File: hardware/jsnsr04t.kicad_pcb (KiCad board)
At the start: 2 copper layers, 50 x 25 mm, 12 parts, among them J1 SWD, J2 MOD_L, J3 JSN-SR04T, J4 MOD_R, U2 DS18B20, U3 5V LDO, U4 TXB0104D, U5 ATtiny1614-SS

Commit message: Route PCB
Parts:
- added G***: LOGO, Logos:logo-pollex-15mm, F.Cu at (108.6, 122.6)
- moved U3 25.1 mm to (138.8, 111.0), turned to 180 degrees
- moved C2 19.9 mm to (136.8, 108.4), turned to 180 degrees
- moved C3 19.7 mm to (135.8, 111.1), turned to 90 degrees
- moved U2 9.00 mm to (134.5, 118.5)
- moved J3 4.00 mm to (124.0, 106.5)
- moved C4 3.35 mm to (116.3, 119.5), turned to 0 degrees
- moved R1 2.52 mm to (125.6, 119.4), turned to 180 degrees
- moved U4 2.50 mm to (121.5, 114.0)
- moved U5 1.73 mm to (113.0, 114.0)
- moved J1 1.07 mm to (107.3, 103.4)
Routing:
- net +3V3: track 0.00 -> 67.7 mm
- net /5V_EN: track 0.00 -> 47.8 mm, vias 0 -> 2
- net +5V?: track 0.00 -> 31.8 mm
- net /SMBALERT: track 0.00 -> 20.1 mm
- net /UPDI: track 0.00 -> 15.5 mm
- net /OneWire_High: track 0.00 -> 14.7 mm
- net GND: track 0.00 -> 12.3 mm, vias 0 -> 8
- net /I2C_SCL: track 0.00 -> 11.4 mm
- net /UART_RX_High: track 0.00 -> 8.90 mm
- net /I2C_SDA: track 0.00 -> 7.18 mm
- net /UART_TX_High: track 0.00 -> 6.58 mm
- net +BATT: track 0.00 -> 6.11 mm
- net /UART_RX_Low: track 0.00 -> 4.08 mm
- net /UART_TX_Low: track 0.00 -> 4.08 mm
- net /OneWire_Low: track 0.00 -> 4.08 mm
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- added copper zone on B.Cu, net GND
- added copper zone on F.Cu, net GND
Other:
- board text added: "+3V3"
- board text added: "ALERT"
- board text added: "DS18B20"
- board text added: "GND"
- board text added: "JSN SR04T"
- board text added: "JSN-SR04T"
- board text added: "SCL"
- board text added: "SDA"
- board text added: "VBAT"

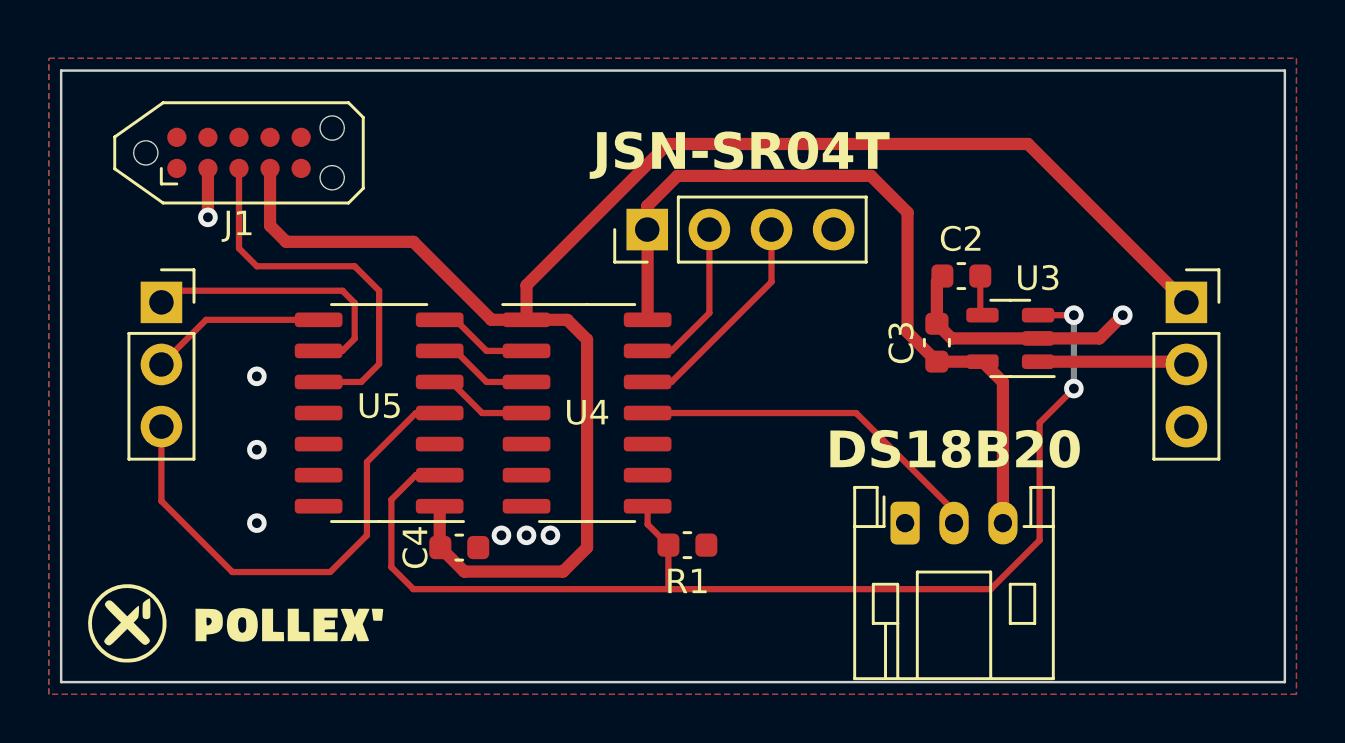
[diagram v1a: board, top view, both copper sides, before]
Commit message: Include terminal blocks for DS18B20
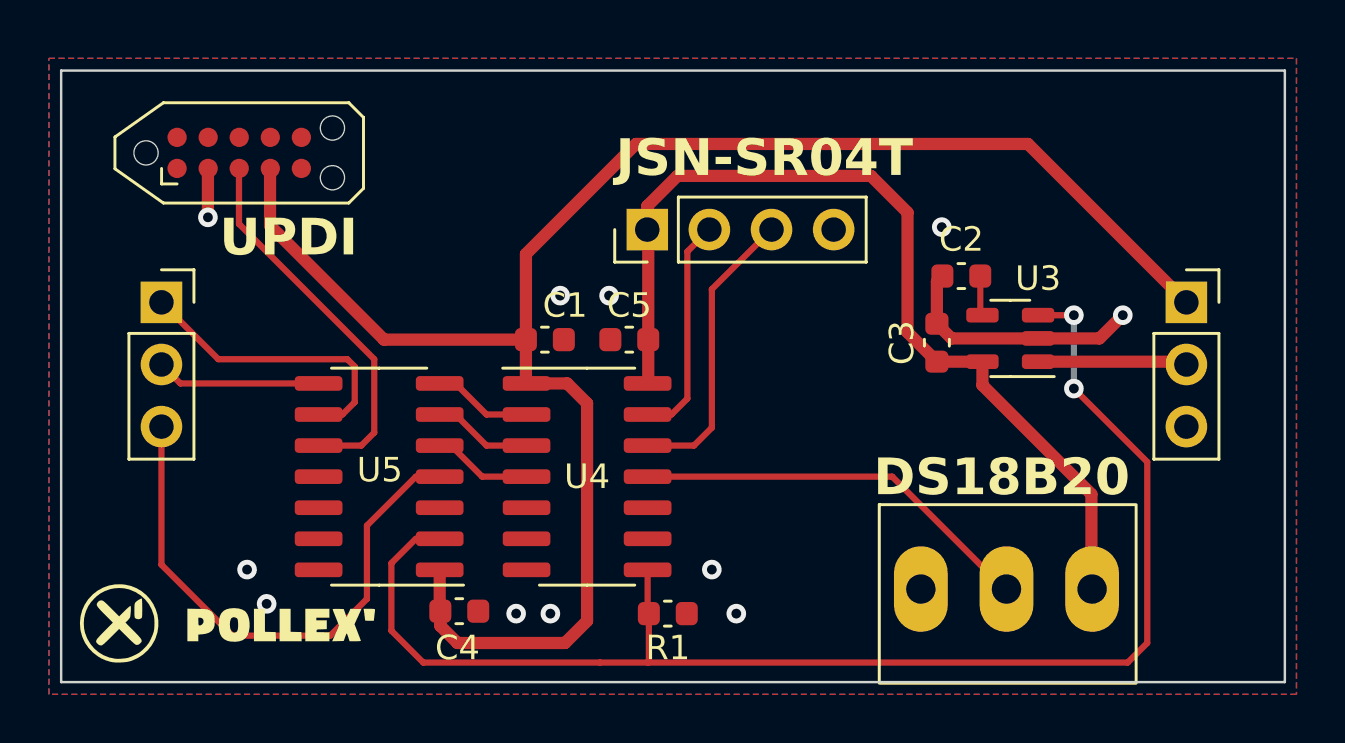
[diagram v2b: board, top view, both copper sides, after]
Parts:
- added C1: 100n, Capacitor_SMD:C_0603_1608Metric, F.Cu at (119.8, 111.0)
- added C5: 100n, Capacitor_SMD:C_0603_1608Metric, F.Cu at (123.2, 111.0)
- U2: footprint Connector_JST:JST_PH_S3B-PH-K_1x03_P2.00mm_Horizontal -> Library:TE-Connectivity_3_pin_terminal_block
- moved R1 2.91 mm to (124.8, 122.2)
- moved C4 2.60 mm to (116.3, 122.1)
- moved U4 2.60 mm to (121.5, 116.6)
- moved U5 2.60 mm to (113.0, 116.6)
- moved U2 1.30 mm to (133.4, 117.7)
- moved G*** 0.33 mm to (108.3, 122.6)
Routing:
- net /5V_EN: track 47.8 -> 56.8 mm
- net +5V?: track 31.8 -> 38.7 mm
- net +3V3: track 67.7 -> 72.3 mm
- net /UART_RX_High: track 8.90 -> 12.0 mm
- net /UART_TX_High: track 6.58 -> 9.18 mm
- net /SMBALERT: track 20.1 -> 22.7 mm
- net /OneWire_High: track 14.7 -> 16.6 mm
- net /I2C_SCL: track 11.4 -> 12.1 mm
- net GND: vias 8 -> 11
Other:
- board text added: "UPDI"

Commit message: Drive DS18B20 from IO Port\nRemove DS18B20 from level translator
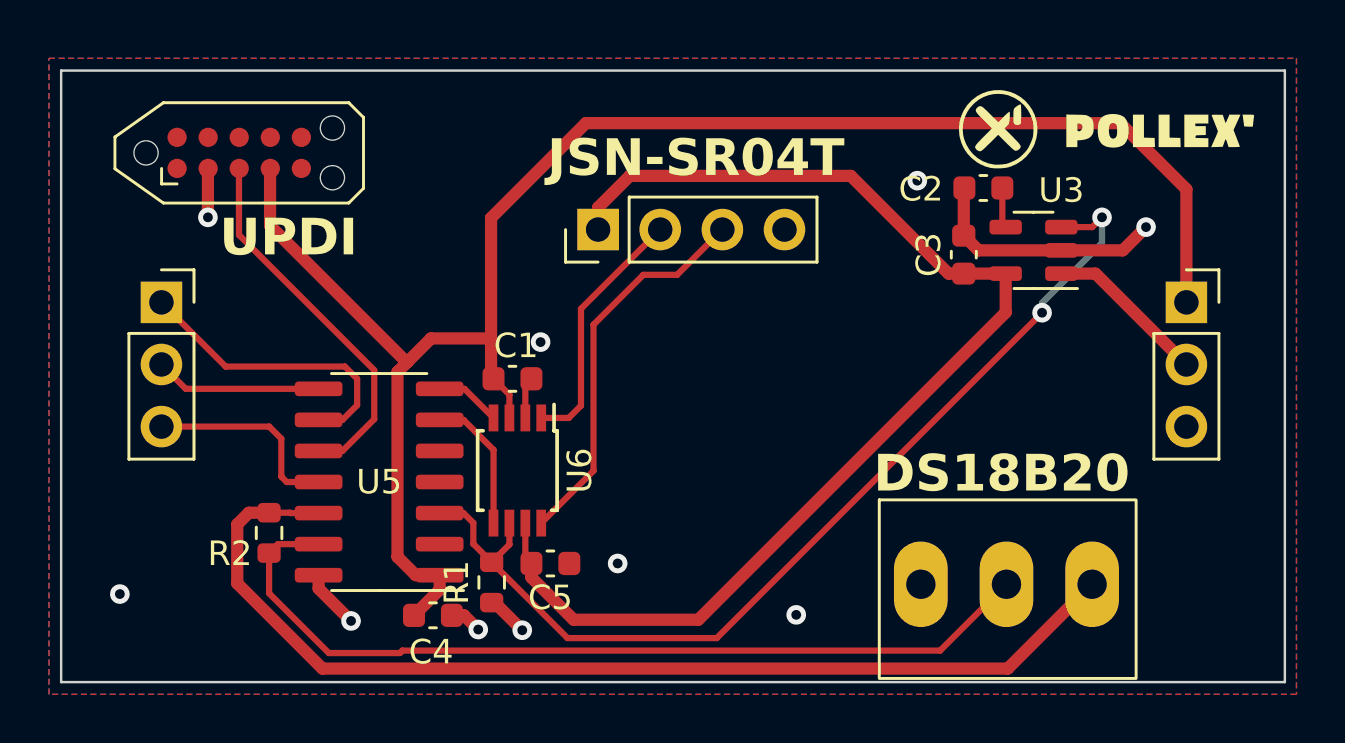
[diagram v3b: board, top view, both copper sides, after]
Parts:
- removed U4: TXB0104D, Package_SO:SOIC-14_3.9x8.7mm_P1.27mm
- added R2: 4k7, Resistor_SMD:R_0603_1608Metric, F.Cu at (108.5, 118.9)
- added U6: TXB0102DCT, Package_SO:TSSOP-8_3x3mm_P0.65mm, F.Cu at (118.7, 116.3)
- R1: footprint Capacitor_SMD:C_0603_1608Metric -> Resistor_SMD:R_0603_1608Metric
- moved G*** 41.2 mm to (144.2, 102.4)
- moved C5 9.70 mm to (120.0, 120.2), turned to 0 degrees
- moved R1 7.31 mm to (117.6, 120.9), turned to 90 degrees
- moved C3 3.76 mm to (136.9, 107.5)
- moved U3 3.72 mm to (139.8, 107.3)
- moved C2 3.71 mm to (137.7, 104.8)
- moved C1 2.08 mm to (118.5, 112.6)
- moved J3 2.01 mm to (122.0, 106.5)
- moved C4 1.09 mm to (115.2, 122.3)
- moved U5 0.22 mm to (113.0, 116.8)
- moved U2 0.20 mm to (133.4, 117.5)
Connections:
- U2 pad 2: /OneWire_High -> /OneWire_Low
- U2 pad 3: +5V? -> /OW_VCC
- U5 pad 11: unconnected-(U5-PA1-Pad11) -> /SMBALERT
- U5 pad 12: unconnected-(U5-PA2-Pad12) -> /OW_VCC
- U5 pad 13: unconnected-(U5-PA3-Pad13) -> /OneWire_Low
- U5 pad 2: /5V_EN -> unconnected-(U5-PA4-Pad2)
- U5 pad 3: unconnected-(U5-PA5-Pad3) -> /5V_EN
- U5 pad 4: /SMBALERT -> unconnected-(U5-PA6-Pad4)
- U5 pad 5: /OneWire_Low -> unconnected-(U5-PA7-Pad5)
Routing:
- net /OW_VCC: track 0.00 -> 43.8 mm
- net /OneWire_Low: track 4.08 -> 37.7 mm
- net /OneWire_High: track 16.6 -> 0.00 mm
- net /5V_EN: track 56.8 -> 41.4 mm
- net /SMBALERT: track 22.7 -> 8.27 mm
- net +5V?: track 38.7 -> 49.0 mm
- net GND: track 12.3 -> 19.2 mm, vias 11 -> 10
- net /UART_RX_High: track 12.0 -> 15.9 mm
- net /UART_RX_Low: track 4.08 -> 5.70 mm
- net +3V3: track 72.3 -> 70.7 mm
- net /UART_TX_Low: track 4.08 -> 2.69 mm
- net /UART_TX_High: track 9.18 -> 10.4 mm
- net +BATT: track 6.11 -> 6.65 mm
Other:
- board text added: "+"
- board text added: "DQ"
